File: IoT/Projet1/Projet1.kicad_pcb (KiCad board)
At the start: 2 copper layers, 50 x 50 mm, 27 parts, among them J1 6120XX21621_61202021621, J2 USB4105GFA060, J3 B2B-XH-A_LF__SN_, U1 MCP73831T-2DCI_MC, U2 MCP1825S-3302E_DB, U3 ESP32-WROOM-32D, U4 TMP117MAIDRVR

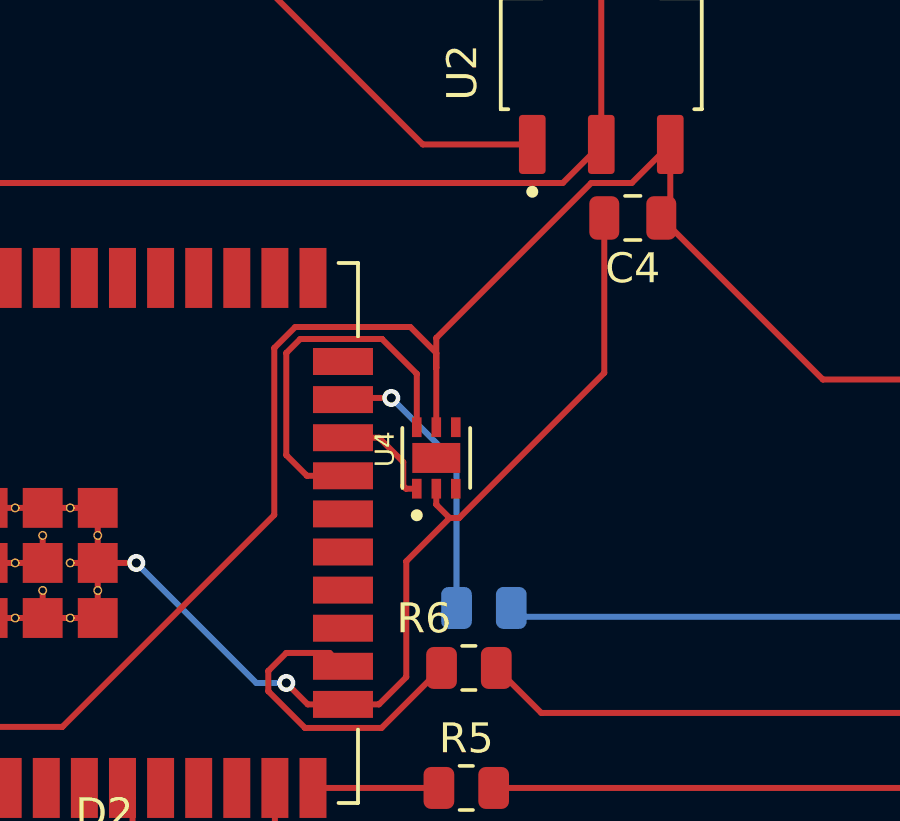
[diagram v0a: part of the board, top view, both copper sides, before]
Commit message: Ajout R_up I2C
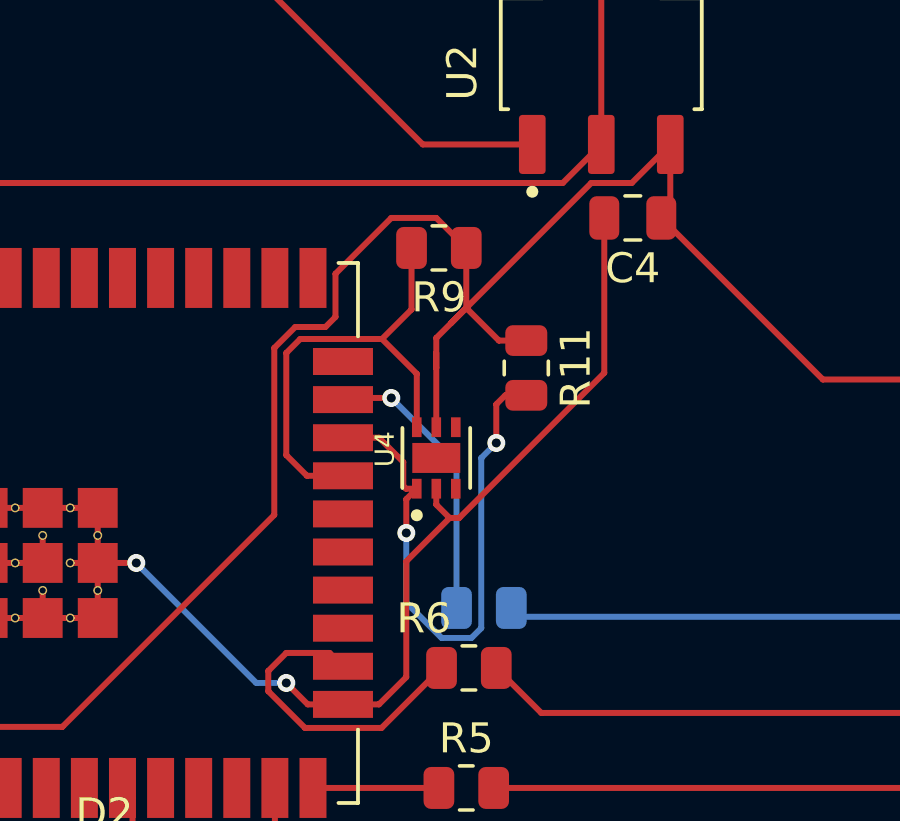
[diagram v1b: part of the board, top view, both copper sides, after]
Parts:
- added R11: 10k, Resistor_SMD:R_0805_2012Metric, F.Cu at (122.0, 131.0)
- added R9: 10k, Resistor_SMD:R_0805_2012Metric, F.Cu at (119.1, 127.0)
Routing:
- net Net-(U3-SDI/SD1): track 3.63 -> 19.5 mm, vias 0 -> 2
- net +3.3V: track 100.5 -> 109.1 mm
- net Net-(U3-SDO/SD0): track 12.4 -> 15.8 mm

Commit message: Ajout plan de masse
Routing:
- added copper zone on B.Cu, net GNDPWR
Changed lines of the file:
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@@
 		(net 58)
 	)
+	(zone
+		(net 3)
+		(net_name "GNDPWR")
+		(layer "B.Cu")
+		(hatch edge 0.5)
+		(connect_pads
+			(clearance 0.5)
+		)
+		(min_thickness 0.25)
+		(filled_areas_thickness no)
+		(fill yes
+			(thermal_gap 0.5)
+			(thermal_bridge_width 0.5)
+		)
+		(polygon
+			(pts
+				(xy 146 101.5) (xy 96 101.5) (xy 96 151.5) (xy 146 151.5)
+			)
+		)
+	)
 )
